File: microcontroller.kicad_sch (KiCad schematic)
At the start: 13 parts, among them SW3 System Reset, SW4 Boot Switch, U1 STM32F446RETx

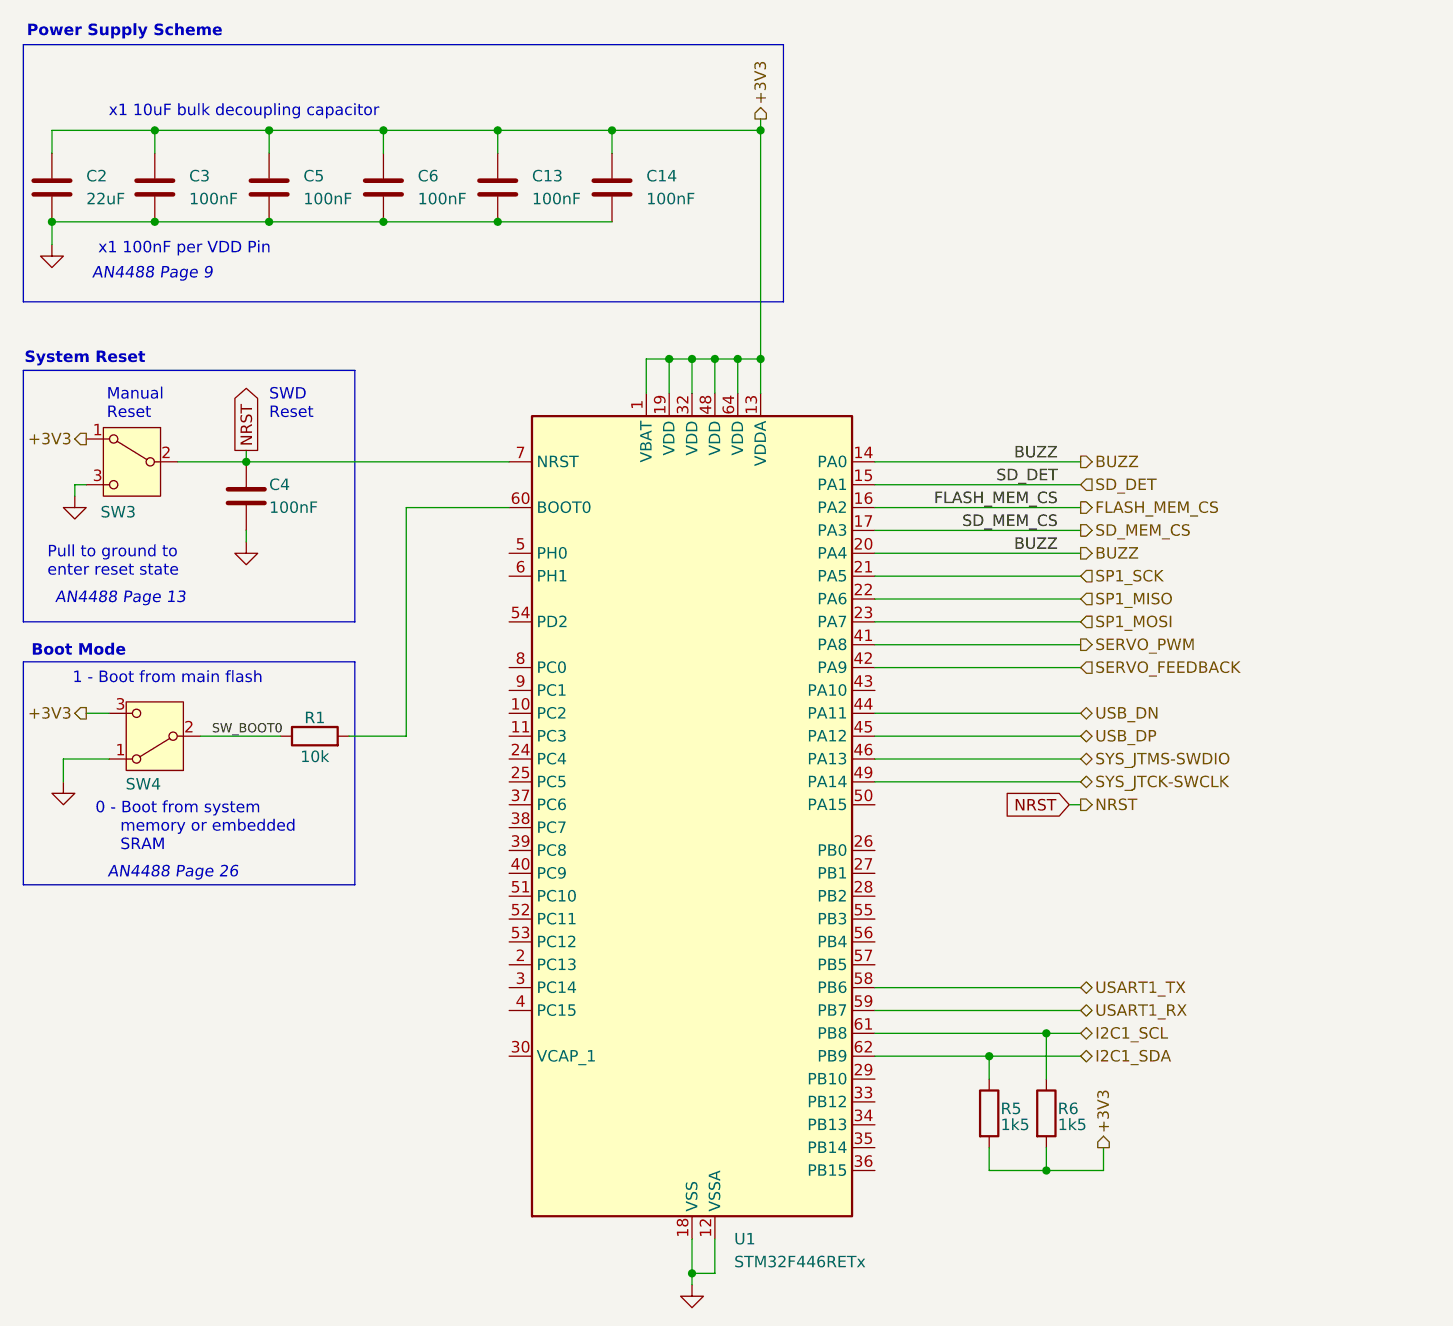
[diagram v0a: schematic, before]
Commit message: Update MCU schematic with VCAP capacitor. Draw boxes around communication busses and programming bus
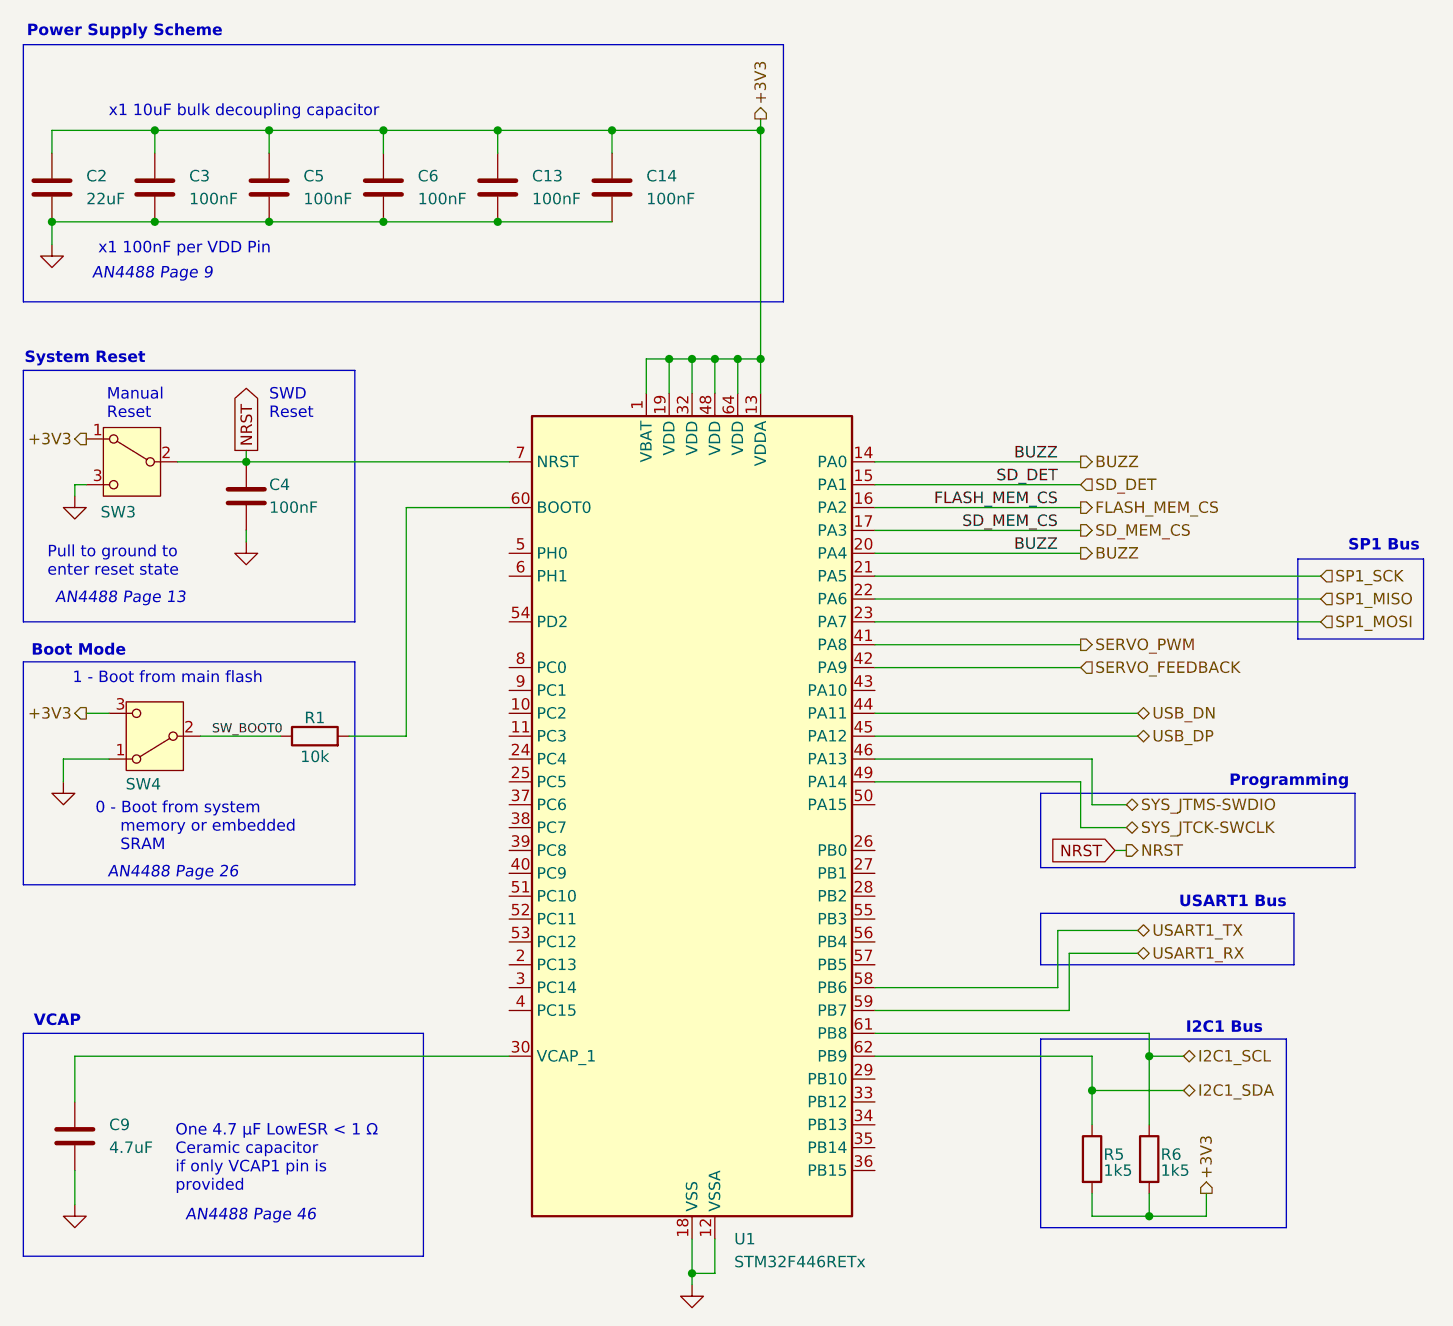
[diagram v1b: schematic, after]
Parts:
- added C9: 4.7uF, Capacitor_SMD:C_0805_2012Metric, symbol Device:C
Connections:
- net GND: now also C9.2
- net at U1.30 (VCAP_1): now also C9.1
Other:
- note added: "AN4488 Page 46"
- note added: "I2C1 Bus"
- note added: "One 4.7 μF LowESR < 1 Ω Ceramic capacitor if only VCAP1 pin is provided"
- note added: "Programming"
- note added: "SP1 Bus"
- note added: "USART1 Bus"
- note added: "VCAP"
- moved on the sheet: R5, R6

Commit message: remove redundant BUZZ pin from PA4
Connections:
- net BUZZ: no longer U1.20 (PA4)
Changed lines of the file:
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@@
-	(wire
-		(pts
-			(xy 146.05 82.55) (xy 168.91 82.55)
-		)
-		(stroke
-			(width 0)
-			(type default)
-		)
-	)
 	(wire
 		(pts
@@
 	(label "SD_DET"
 		(at 166.37 74.93 180)
-		(effects
-			(font
-				(size 1.27 1.27)
-			)
-			(justify right bottom)
-		)
-	)
-	(label "BUZZ"
-		(at 166.37 82.55 180)
 		(effects
 			(font
@@
 		(effects
 			(font
-				(size 1.27 1.27)
-			)
-			(justify left)
-		)
-	)
-	(hierarchical_label "BUZZ"
-		(shape output)
-		(at 168.91 82.55 0)
-		(effects
-			(font
